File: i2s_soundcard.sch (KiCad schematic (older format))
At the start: 13 parts, among them J1 Conn_01x08, J2 Conn_01x06, J3 Conn_01x05, J4 Conn_01x11, J5 Conn_01x04, U1 TLV320AIC3104IRHBT, U6 TLV7111830DSER, U7 TPD4E02B04DQAR, U8 TPD4E02B04DQAR

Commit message: Capitalize net names
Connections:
- net labels added: BCLK, DETECT?, DIN, DOUT, EN1, EN2, INTMIC_N, INTMIC_P, IOVDD, LOL_N, LOL_P, LOR_N, LOR_P, MCLK, MUTE, RESET, RING1, RING2, RING2_AGAIN, SCA, SCL, SEL, SLEEVE, TIP, VBAT_3.7, VCC1.8, VCC3.3, WCLK, ~SHUTDOWN
- net labels removed: LOL+, LOL-, LOR+, LOR-, bclk, detect?, din, dout, en1, en2, intmic+, intmic-, iovdd, mclk, mute, reset, ring1, ring2, ring2_again, sca, scl, sel, sleeve, tip, v1.8, v3.3, vbat, wclk, ~shutdown
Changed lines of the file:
@@
 $EndComp
 Text Label 6850 5500 2    50   ~ 0
-intmic+
+INTMIC_P
 Text Label 6850 5600 2    50   ~ 0
-intmic-
+INTMIC_N
 Text Label 6850 5700 2    50   ~ 0
-tip
+TIP
 Text Label 6850 5800 2    50   ~ 0
-ring2
+RING2
 Text Label 6850 5900 2    50   ~ 0
-sleeve
+SLEEVE
 Text Label 6850 6000 2    50   ~ 0
-ring2_again
+RING2_AGAIN
 Text Label 6850 6200 2    50   ~ 0
-ring1
+RING1
 Wire Wire Line
 	4000 5500 4000 5100
@@
 Connection ~ 2800 950
 Text Label 3700 750  0    50   ~ 0
-v1.8
+VCC1.8
 Text Label 3700 850  0    50   ~ 0
-v3.3
+VCC3.3
 Wire Wire Line
 	5100 2400 5100 2500
 Text Label 1100 1650 1    50   ~ 0
-vbat
+VBAT_3.7
 Text Label 1200 1650 1    50   ~ 0
-en2
+EN2
 Text Label 1000 1650 1    50   ~ 0
-en1
+EN1
 Text Label 7450 2800 2    50   ~ 0
-vbat
+VBAT_3.7
 $Comp
 L Connector_Generic:Conn_01x11 J4
@@
 $EndComp
 Text Label 2650 3250 0    50   ~ 0
-mclk
+MCLK
 Text Label 2650 3350 0    50   ~ 0
-bclk
+BCLK
 Text Label 2650 3450 0    50   ~ 0
-wclk
+WCLK
 Text Label 2650 3550 0    50   ~ 0
-din
+DIN
 Text Label 2650 3650 0    50   ~ 0
-dout
+DOUT
 Text Label 2650 3750 0    50   ~ 0
-scl
+SCL
 Text Label 2650 3850 0    50   ~ 0
-sca
+SCA
 Text Label 1800 2450 0    50   ~ 0
-iovdd
+IOVDD
 Text Label 9400 2900 0    50   ~ 0
-LOR+
+LOR_P
 Text Label 9400 3000 0    50   ~ 0
-LOR-
+LOR_N
 Text Label 9400 3200 0    50   ~ 0
-LOL-
+LOL_N
 Text Label 9400 3100 0    50   ~ 0
-LOL+
+LOL_P
 Text Label 7350 4400 1    50   ~ 0
-~shutdown
+~SHUTDOWN
 Text Label 7250 4500 1    50   ~ 0
-sel
+SEL
 Text Label 7150 4600 1    50   ~ 0
-mute
+MUTE
 Text Label 2450 3050 0    50   ~ 0
-mute
+MUTE
 Text Label 2450 2950 0    50   ~ 0
-sel
+SEL
 Text Label 2450 2850 0    50   ~ 0
-~shutdown
+~SHUTDOWN
 Text Label 2600 3150 0    50   ~ 0
-reset
+RESET
 Wire Wire Line
 	2450 3850 2750 3850
@@
 Connection ~ 8350 5500
 Text Label 6850 6100 2    50   ~ 0
-detect?
+DETECT?
 Wire Wire Line
 	7600 6400 7700 6400

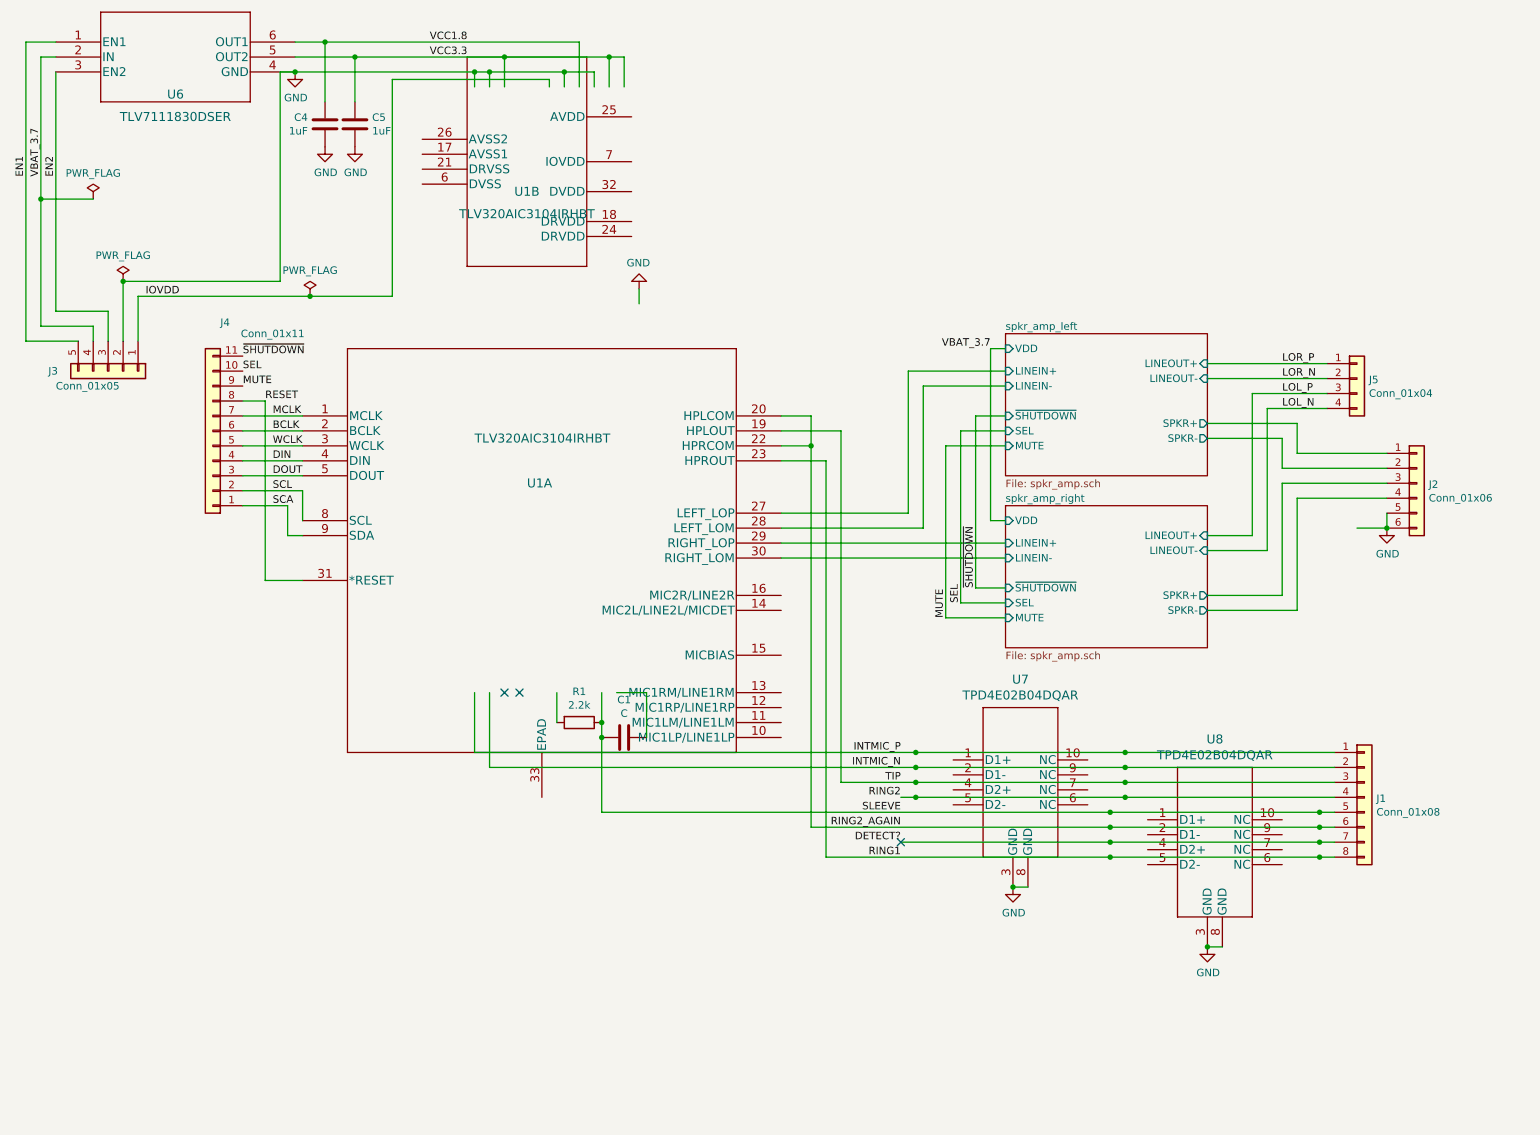
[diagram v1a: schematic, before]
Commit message: Rearrange pins on codec, TVS diodes, clean up schematic a bit.
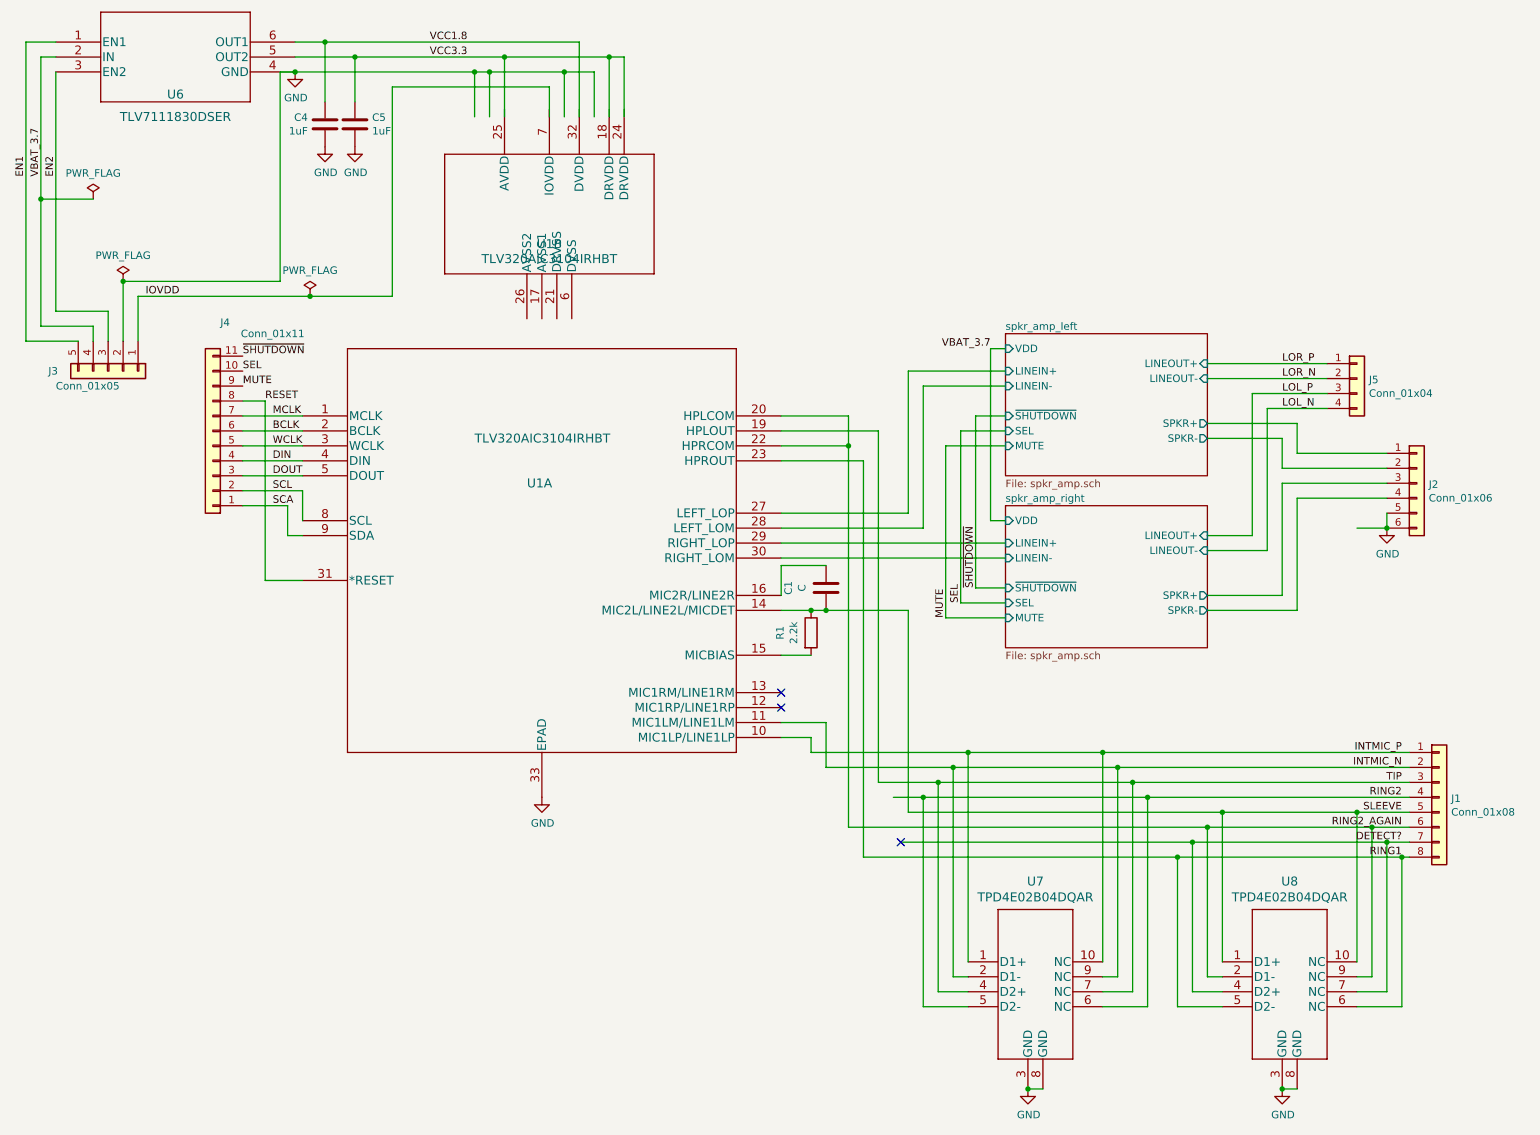
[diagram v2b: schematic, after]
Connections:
- wire segments 140 -> 170
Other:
- moved on the sheet: C1, J1, R1, U1B, U7, U8

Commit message: Lots of schematic cleanup and board tweaking
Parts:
- added C10: 10uF, Capacitor_SMD:C_0402_1005Metric, symbol Device:C
- added C11: 100nF, Capacitor_SMD:C_0402_1005Metric, symbol Device:C
- added C8: 0.1uF, Capacitor_SMD:C_0402_1005Metric, symbol Device:C
- added C9: 220nF, Capacitor_SMD:C_0402_1005Metric, symbol Device:C
- C4: value 1uF -> 10uF
- C5: value 1uF -> 22uF
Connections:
- net labels added: VCC3.0
- net labels removed: VCC3.3
- wire segments 170 -> 172
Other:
- moved on the sheet: C4, C5, J3, U1B

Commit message: AC-couple headphone outputs. This frees up HPRCOM and HPLCOM, which I can use for line outputs, since the dock line out is single-ended anyway.
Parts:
- removed J5: Conn_01x04, Connector_PinHeader_1.00mm:PinHeader_1x04_P1.00mm_Vertical, symbol Connector_Generic:Conn_01x04
- added C2, C3: C, Capacitor_SMD:C_0402_1005Metric, symbol Device:C
- added J5: Conn_01x03, Connector_PinHeader_1.00mm:PinHeader_1x03_P1.00mm_Vertical, symbol Connector_Generic:Conn_01x03
- J3: value Conn_01x05 -> Conn_01x04; footprint Connector_PinHeader_1.00mm:PinHeader_1x05_P1.00mm_Vertical -> Connector_PinHeader_1.00mm:PinHeader_1x04_P1.00mm_Vertical; symbol Connector_Generic:Conn_01x05 -> Connector_Generic:Conn_01x04
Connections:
- net labels added: LOL, LOR
- net labels removed: LOL_N, LOL_P, LOR_N, LOR_P, MUTE, SEL
- wire segments 172 -> 149
- no-connect marks 3 -> 4
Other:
- moved on the sheet: J4
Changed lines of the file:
@@
 F6 "LINEIN+" I L 7550 2950 50
 F7 "LINEIN-" I L 7550 3050 50
-F8 "SEL" I L 7550 3350 50
-F9 "LINEOUT+" I R 8900 2900 50
-F10 "LINEOUT-" I R 8900 3000 50
-F11 "MUTE" I L 7550 3450 50
 $EndSheet
 $Sheet
@@
 F6 "LINEIN+" I L 7550 4100 50
 F7 "LINEIN-" I L 7550 4200 50
-F8 "SEL" I L 7550 4500 50
-F9 "LINEOUT+" I R 8900 4050 50
-F10 "LINEOUT-" I R 8900 4150 50
-F11 "MUTE" I L 7550 4600 50
 $EndSheet
 Wire Wire Line
@@
 Wire Wire Line
 	7450 2800 7550 2800
-Wire Wire Line
-	7550 4500 7250 4500
-Wire Wire Line
-	7250 4500 7250 3350
-Wire Wire Line
-	7250 3350 7550 3350
-Wire Wire Line
-	7550 3450 7150 3450
-Wire Wire Line
-	7150 3450 7150 4600
-Wire Wire Line
-	7150 4600 7550 4600
 Wire Wire Line
 	7550 4400 7350 4400
@@
 Wire Wire Line
 	6350 5600 6350 5300
-Wire Wire Line
-	6700 5700 6700 3350
-Wire Wire Line
-	6700 3350 6050 3350
-Wire Wire Line
-	6050 3550 6600 3550
-Wire Wire Line
-	6600 3550 6600 6200
-Wire Wire Line
-	6500 6000 6500 3450
-Wire Wire Line
-	6500 3450 6050 3450
-Wire Wire Line
-	6500 3450 6500 3250
-Wire Wire Line
-	6500 3250 6050 3250
-Connection ~ 6500 3450
 $Comp
 L Device:R R1
@@
 Wire Wire Line
 	6350 4550 6900 4550
-NoConn ~ 6850 6100
 $Comp
 L TLV7111830DSER:TLV7111830DSER U6
@@
 Text Label 7450 2800 2    50   ~ 0
 VBAT_3.7
-$Comp
-L Connector_Generic:Conn_01x04 J5
-U 1 1 6037CBEB
-P 9900 3000
-F 0 "J5" H 9980 2992 50  0000 L CNN
-F 1 "Conn_01x04" H 9980 2901 50  0000 L CNN
-F 2 "Connector_PinHeader_1.00mm:PinHeader_1x04_P1.00mm_Vertical" H 9900 3000 50  0001 C CNN
-F 3 "~" H 9900 3000 50  0001 C CNN
-	1    9900 3000
-	1    0    0    -1
-$EndComp
-Wire Wire Line
-	8900 4150 9300 4150
-Wire Wire Line
-	9300 4150 9300 3200
-Wire Wire Line
-	9300 3200 9700 3200
-Wire Wire Line
-	9700 3100 9200 3100
-Wire Wire Line
-	9200 3100 9200 4050
-Wire Wire Line
-	9200 4050 8900 4050
-Wire Wire Line
-	8900 3000 9700 3000
-Wire Wire Line
-	9700 2900 8900 2900
 Wire Wire Line
 	1650 2350 1650 2600
-Text Label 1800 2450 0    50   ~ 0
+Text Label 1350 3850 0    50   ~ 0
 IOVDD
-Text Label 9400 2900 0    50   ~ 0
-LOR_P
-Text Label 9400 3000 0    50   ~ 0
-LOR_N
-Text Label 9400 3200 0    50   ~ 0
-LOL_N
-Text Label 9400 3100 0    50   ~ 0
-LOL_P
 Text Label 7350 4400 1    50   ~ 0
 ~SHUTDOWN
-Text Label 7250 4500 1    50   ~ 0
-SEL
-Text Label 7150 4600 1    50   ~ 0
-MUTE
-Wire Wire Line
-	1750 2950 1750 2450
-Wire Wire Line
-	1750 2450 2150 2450
+Wire Wire Line
+	1300 3850 1700 3850
 $Comp
 L TPD4E02B04DQAR:TPD4E02B04DQAR U7
@@
 L power:PWR_FLAG #FLG0103
 U 1 1 6062ECA7
-P 2150 2450
-F 0 "#FLG0103" H 2150 2525 50  0001 C CNN
-F 1 "PWR_FLAG" H 2150 2623 50  0000 C CNN
-F 2 "" H 2150 2450 50  0001 C CNN
-F 3 "~" H 2150 2450 50  0001 C CNN
-	1    2150 2450
+P 1700 3850
+F 0 "#FLG0103" H 1700 3925 50  0001 C CNN
+F 1 "PWR_FLAG" H 1700 4023 50  0000 C CNN
+F 2 "" H 1700 3850 50  0001 C CNN
+F 3 "~" H 1700 3850 50  0001 C CNN
+	1    1700 3850
 	1    0    0    -1
 $EndComp
@@
 Connection ~ 7700 7750
 Wire Wire Line
-	6600 6200 8700 6200
-Wire Wire Line
-	6500 6000 8900 6000
+	6850 6200 8700 6200
+Wire Wire Line
+	6850 6000 8900 6000
 Wire Wire Line
 	6850 6100 8800 6100
@@
 	7100 5700 8400 5700
 Wire Wire Line
-	7300 7200 7000 7200
-Wire Wire Line
-	7000 7200 7000 5800
-Wire Wire Line
-	7000 5800 8500 5800
-Wire Wire Line
 	8200 6900 8200 5500
 Connection ~ 8200 5500
@@
 Connection ~ 8400 5700
 Wire Wire Line
-	8200 7200 8500 7200
-Wire Wire Line
-	8500 7200 8500 5800
-Connection ~ 8500 5800
-Wire Wire Line
 	8200 5500 10250 5500
 Wire Wire Line
@@
 Wire Wire Line
 	8400 5700 10250 5700
-Wire Wire Line
-	8500 5800 10250 5800
 Wire Wire Line
 	9000 6900 9000 5900
@@
 	10200 6200 10250 6200
 Wire Wire Line
-	6700 5700 7100 5700
+	6850 5700 7100 5700
 Wire Wire Line
 	6350 5600 7200 5600
@@
 	6900 5900 9000 5900
 Wire Wire Line
-	7000 5800 6800 5800
-Connection ~ 7000 5800
-Wire Wire Line
 	6350 5300 6050 5300
 Wire Wire Line
@@
 	6250 5400 6050 5400
 Wire Wire Line
-	2850 3950 2850 3750
+	2850 3950 2450 3950
 $Comp
 L TLV320AIC3104IRHBT:TLV320AIC3104IRHBT U1
@@
 Wire Wire Line
 	2450 3650 2850 3650
-Wire Wire Line
-	2450 3750 2850 3750
-Wire Wire Line
-	2450 3850 2750 3850
-Text Label 2600 3150 0    50   ~ 0
-RESET
-Text Label 2450 2850 0    50   ~ 0
-~SHUTDOWN
-Text Label 2450 2950 0    50   ~ 0
-SEL
-Text Label 2450 3050 0    50   ~ 0
-MUTE
-Text Label 2650 3850 0    50   ~ 0
+Text Label 2650 4050 0    50   ~ 0
 SCA
-Text Label 2650 3750 0    50   ~ 0
+Text Label 2650 3950 0    50   ~ 0
 SCL
 Text Label 2650 3650 0    50   ~ 0
@@
 Text Label 2650 3250 0    50   ~ 0
 MCLK
-Wire Wire Line
-	2750 4050 2750 3850
-Wire Wire Line
-	2850 4050 2750 4050
-$Comp
-L Connector_Generic:Conn_01x11 J4
-U 1 1 6035D713
-P 2250 3350
-F 0 "J4" H 2168 2625 50  0000 C CNN
-F 1 "Conn_01x11" H 1850 2700 50  0000 C CNN
-F 2 "Connector_PinHeader_1.00mm:PinHeader_1x11_P1.00mm_Vertical" H 2250 3350 50  0001 C CNN
-F 3 "~" H 2250 3350 50  0001 C CNN
-	1    2250 3350
-	-1   0    0    1
-$EndComp
 $Comp
 L power:GND #PWR0110
@@
 	4450 950  4450 1100
 $Comp
-L Connector_Generic:Conn_01x05 J3
+L Connector_Generic:Conn_01x04 J3
 U 1 1 60399FB4
 P 1550 3150
 F 0 "J3" V 1550 2750 50  0000 L CNN
-F 1 "Conn_01x05" V 1650 2800 50  0000 L CNN
-F 2 "Connector_PinHeader_1.00mm:PinHeader_1x05_P1.00mm_Vertical" H 1550 3150 50  0001 C CNN
+F 1 "Conn_01x04" V 1650 2800 50  0000 L CNN
+F 2 "Connector_PinHeader_1.00mm:PinHeader_1x04_P1.00mm_Vertical" H 1550 3150 50  0001 C CNN
 F 3 "~" H 1550 3150 50  0001 C CNN
 	1    1550 3150
@@
 Wire Wire Line
 	1000 2750 1000 750
+Text Label 6700 3550 2    50   ~ 0
+RING1
+$Comp
+L Device:C C3
+U 1 1 6033DCEF
+P 6400 3550
+F 0 "C3" V 6148 3550 50  0000 C CNN
+F 1 "C" V 6250 3550 50  0000 C CNN
+F 2 "Capacitor_SMD:C_0402_1005Metric" H 6438 3400 50  0001 C CNN
+F 3 "~" H 6400 3550 50  0001 C CNN
+	1    6400 3550
+	0    1    -1   0
+$EndComp
+$Comp
+L Device:C C2
+U 1 1 6033EBF1
+P 6400 3350
+F 0 "C2" V 6148 3350 50  0000 C CNN
+F 1 "C" V 6239 3350 50  0000 C CNN
+F 2 "Capacitor_SMD:C_0402_1005Metric" H 6438 3200 50  0001 C CNN
+F 3 "~" H 6400 3350 50  0001 C CNN
+	1    6400 3350
+	0    -1   1    0
+$EndComp
+Wire Wire Line
+	6550 3550 6700 3550
+Wire Wire Line
+	6550 3350 6700 3350
+Wire Wire Line
+	6250 3350 6050 3350
+Wire Wire Line
+	6250 3550 6050 3550
+$Comp
+L power:GND #PWR04
+U 1 1 603EA5D4
+P 6300 5800
+F 0 "#PWR04" H 6300 5550 50  0001 C CNN
+F 1 "GND" H 6305 5627 50  0000 C CNN
+F 2 "" H 6300 5800 50  0001 C CNN
+F 3 "" H 6300 5800 50  0001 C CNN
+	1    6300 5800
+	1    0    0    -1
+$EndComp
+Text Label 6800 4550 2    50   ~ 0
+SLEEVE
+Text Label 6700 3350 2    50   ~ 0
+TIP
+$Comp
+L Connector_Generic:Conn_01x03 J5
+U 1 1 6042168E
+P 6150 2650
+F 0 "J5" V 6114 2462 50  0000 R CNN
+F 1 "Conn_01x03" V 6023 2462 50  0000 R CNN
+F 2 "Connector_PinHeader_1.00mm:PinHeader_1x03_P1.00mm_Vertical" H 6150 2650 50  0001 C CNN
+F 3 "~" H 6150 2650 50  0001 C CNN
+	1    6150 2650
+	0    -1   -1   0
+$EndComp
+Wire Wire Line
+	6050 3250 6050 2850
+Wire Wire Line
+	6050 3450 6150 3450
+Wire Wire Line
+	6150 3450 6150 2850
+$Comp
+L power:GND #PWR03
+U 1 1 6043245F
+P 6250 2850
+F 0 "#PWR03" H 6250 2600 50  0001 C CNN
+F 1 "GND" H 6255 2677 50  0000 C CNN
+F 2 "" H 6250 2850 50  0001 C CNN
+F 3 "" H 6250 2850 50  0001 C CNN
+	1    6250 2850
+	1    0    0    -1
+$EndComp
+Wire Wire Line
+	6300 5800 10250 5800
+NoConn ~ 7300 7200
+NoConn ~ 8200 7200
+Text Label 6050 3150 1    50   ~ 0
+LOL
+Text Label 6150 3150 1    50   ~ 0
+LOR
+Text Label 2650 4350 0    50   ~ 0
+RESET
+Text Label 2450 3050 0    50   ~ 0
+~SHUTDOWN
+$Comp
+L Connector_Generic:Conn_01x11 J4
+U 1 1 6035D713
+P 2250 3550
+F 0 "J4" H 2350 3550 50  0000 C CNN
+F 1 "Conn_01x11" H 2250 4100 50  0000 C CNN
+F 2 "Connector_PinHeader_1.00mm:PinHeader_1x11_P1.00mm_Vertical" H 2250 3550 50  0001 C CNN
+F 3 "~" H 2250 3550 50  0001 C CNN
+	1    2250 3550
+	-1   0    0    1
+$EndComp
+Wire Wire Line
+	2450 4050 2850 4050
+Text Label 2650 3850 0    50   ~ 0
+IOVDD
+Wire Wire Line
+	2450 3850 2850 3850
+$Comp
+L power:GND #PWR?
+U 1 1 604C7294
+P 3000 3750
+F 0 "#PWR?" H 3000 3500 50  0001 C CNN
+F 1 "GND" H 3100 3750 50  0000 C CNN
+F 2 "" H 3000 3750 50  0001 C CNN
+F 3 "" H 3000 3750 50  0001 C CNN
+	1    3000 3750
+	1    0    0    -1
+$EndComp
+Wire Wire Line
+	2450 3750 3000 3750
 $EndSCHEMATC

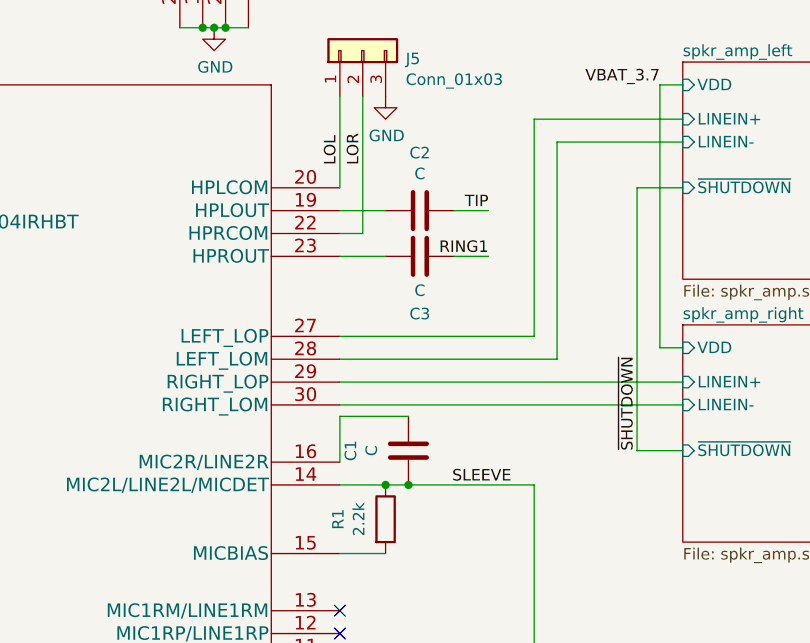
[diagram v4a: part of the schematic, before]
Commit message: Specify values of capacitors
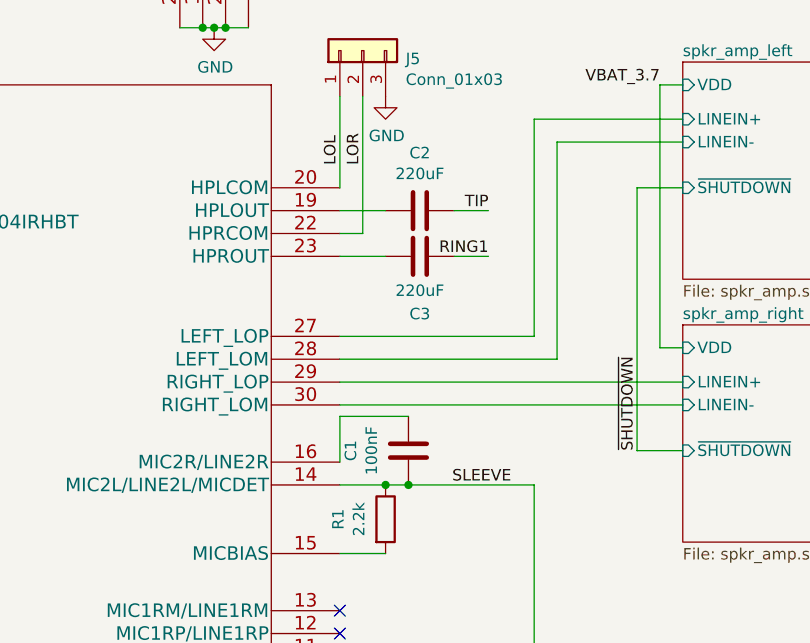
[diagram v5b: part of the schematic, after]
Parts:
- C1: value C -> 100nF
- C2, C3: value C -> 220uF
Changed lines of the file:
@@
 P 6350 4400
 F 0 "C1" V 6098 4400 50  0000 C CNN
-F 1 "C" V 6189 4400 50  0000 C CNN
+F 1 "100nF" V 6189 4400 50  0000 C CNN
 F 2 "Capacitor_SMD:C_0402_1005Metric" H 6388 4250 50  0001 C CNN
 F 3 "~" H 6350 4400 50  0001 C CNN
@@
 P 6400 3550
 F 0 "C3" V 6148 3550 50  0000 C CNN
-F 1 "C" V 6250 3550 50  0000 C CNN
+F 1 "220uF" V 6250 3550 50  0000 C CNN
 F 2 "Capacitor_SMD:C_0402_1005Metric" H 6438 3400 50  0001 C CNN
 F 3 "~" H 6400 3550 50  0001 C CNN
@@
 P 6400 3350
 F 0 "C2" V 6148 3350 50  0000 C CNN
-F 1 "C" V 6239 3350 50  0000 C CNN
+F 1 "220uF" V 6239 3350 50  0000 C CNN
 F 2 "Capacitor_SMD:C_0402_1005Metric" H 6438 3200 50  0001 C CNN
 F 3 "~" H 6400 3350 50  0001 C CNN
@@
 	2450 3850 2850 3850
 $Comp
-L power:GND #PWR?
+L power:GND #PWR0104
 U 1 1 604C7294
 P 3000 3750
-F 0 "#PWR?" H 3000 3500 50  0001 C CNN
+F 0 "#PWR0104" H 3000 3500 50  0001 C CNN
 F 1 "GND" H 3100 3750 50  0000 C CNN
 F 2 "" H 3000 3750 50  0001 C CNN
